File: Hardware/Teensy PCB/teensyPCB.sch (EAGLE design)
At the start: 16 parts, among them U1 HC_05, U2 USD-SOCKETNEW

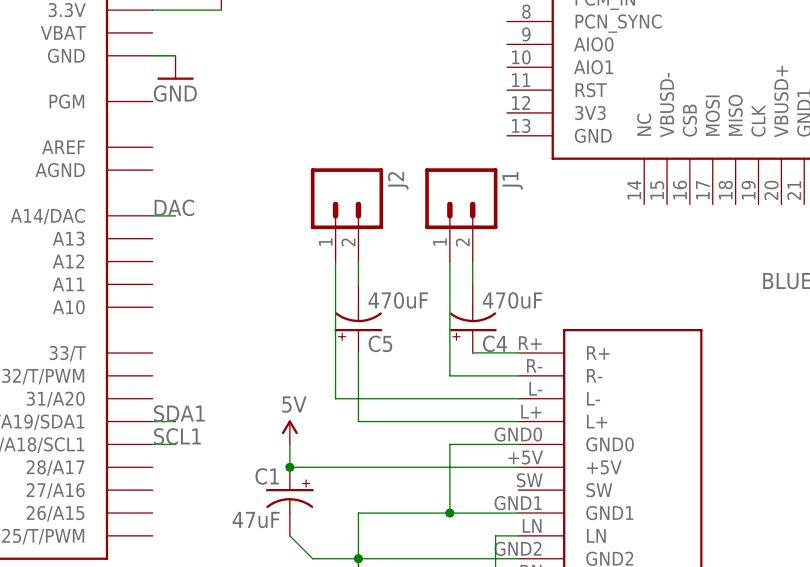
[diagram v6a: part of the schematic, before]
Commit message: Modified audio connections
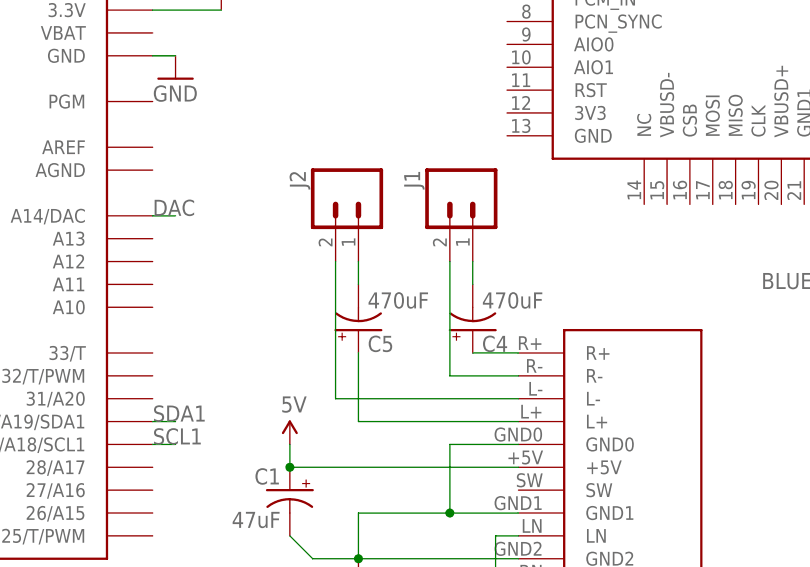
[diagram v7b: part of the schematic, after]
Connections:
- net N$3: now also C5.-, J2.1; no longer C4.-, J1.2
- net N$4: now also C4.-, J1.1; no longer C5.-, J2.2
- net N$6: now also J1.2; no longer J1.1
- net N$7: now also J2.2; no longer J2.1
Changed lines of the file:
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@@
 <setting verticaltext="up"/>
 </settings>
-<grid distance="0.1" unitdist="inch" unit="inch" style="lines" multiple="1" display="yes" altdistance="0.01" altunitdist="inch" altunit="inch"/>
+<grid distance="0.1" unitdist="inch" unit="inch" style="lines" multiple="1" display="no" altdistance="0.01" altunitdist="inch" altunit="inch"/>
 <layers>
 <layer number="1" name="Top" color="4" fill="1" visible="no" active="no"/>
@@
 <instance part="C2" gate="G$1" x="60.96" y="-35.56" rot="R90"/>
 <instance part="C3" gate="G$1" x="60.96" y="-43.18" rot="R90"/>
-<instance part="J1" gate="G$1" x="60.96" y="20.32" rot="R270"/>
-<instance part="J2" gate="G$1" x="48.26" y="20.32" rot="R270"/>
+<instance part="J1" gate="G$1" x="63.5" y="20.32" rot="MR270"/>
+<instance part="J2" gate="G$1" x="50.8" y="20.32" rot="MR270"/>
 <instance part="C4" gate="G$1" x="63.5" y="5.08" rot="MR180"/>
 <instance part="C5" gate="G$1" x="50.8" y="5.08" rot="MR180"/>
@@
 </segment>
 </net>
-<net name="N$3" class="0">
-<segment>
-<pinref part="J1" gate="G$1" pin="2"/>
-<pinref part="C4" gate="G$1" pin="-"/>
-<wire x1="63.5" y1="12.7" x2="63.5" y2="10.16" width="0.1524" layer="91"/>
-</segment>
-</net>
-<net name="N$4" class="0">
-<segment>
-<pinref part="J2" gate="G$1" pin="2"/>
-<pinref part="C5" gate="G$1" pin="-"/>
-<wire x1="50.8" y1="10.16" x2="50.8" y2="12.7" width="0.1524" layer="91"/>
-</segment>
-</net>
 <net name="N$5" class="0">
 <segment>
@@
 <net name="N$6" class="0">
 <segment>
-<pinref part="J1" gate="G$1" pin="1"/>
-<wire x1="60.96" y1="12.7" x2="60.96" y2="0" width="0.1524" layer="91"/>
 <pinref part="U$4" gate="G$1" pin="R-"/>
 <wire x1="60.96" y1="0" x2="68.58" y2="0" width="0.1524" layer="91"/>
+<pinref part="J1" gate="G$1" pin="2"/>
+<wire x1="60.96" y1="12.7" x2="60.96" y2="0" width="0.1524" layer="91"/>
 </segment>
 </net>
@@
 <segment>
 <pinref part="U$4" gate="G$1" pin="L-"/>
-<pinref part="J2" gate="G$1" pin="1"/>
 <wire x1="68.58" y1="-2.54" x2="48.26" y2="-2.54" width="0.1524" layer="91"/>
-<wire x1="48.26" y1="-2.54" x2="48.26" y2="12.7" width="0.1524" layer="91"/>
+<pinref part="J2" gate="G$1" pin="2"/>
+<wire x1="48.26" y1="12.7" x2="48.26" y2="-2.54" width="0.1524" layer="91"/>
 </segment>
 </net>
@@
 </segment>
 </net>
+<net name="N$3" class="0">
+<segment>
+<pinref part="C5" gate="G$1" pin="-"/>
+<pinref part="J2" gate="G$1" pin="1"/>
+<wire x1="50.8" y1="12.7" x2="50.8" y2="10.16" width="0.1524" layer="91"/>
+</segment>
+</net>
+<net name="N$4" class="0">
+<segment>
+<pinref part="C4" gate="G$1" pin="-"/>
+<pinref part="J1" gate="G$1" pin="1"/>
+<wire x1="63.5" y1="12.7" x2="63.5" y2="10.16" width="0.1524" layer="91"/>
+</segment>
+</net>

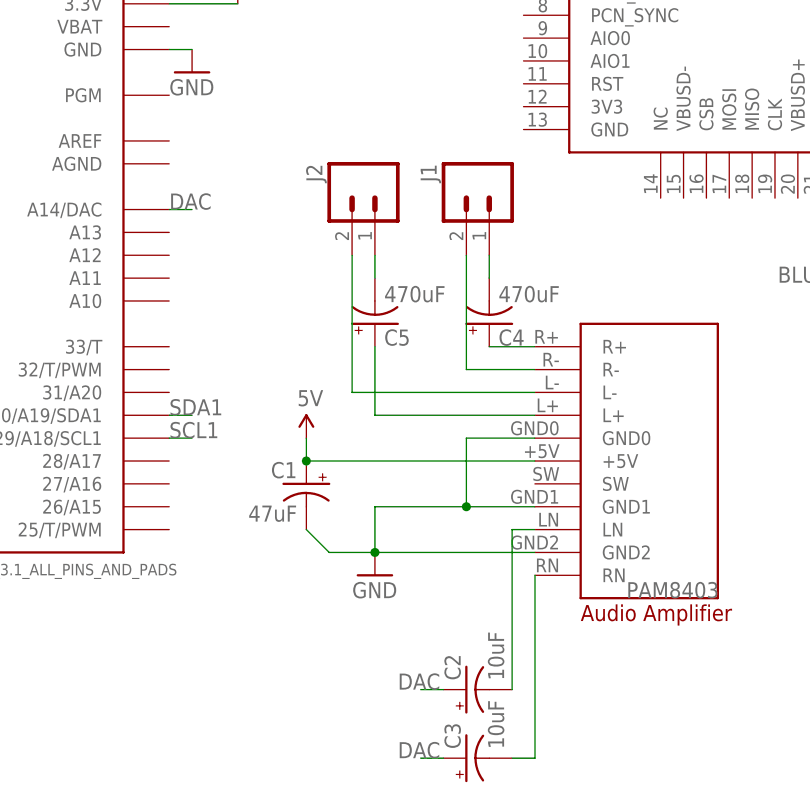
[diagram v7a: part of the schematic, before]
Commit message: Modified audio component
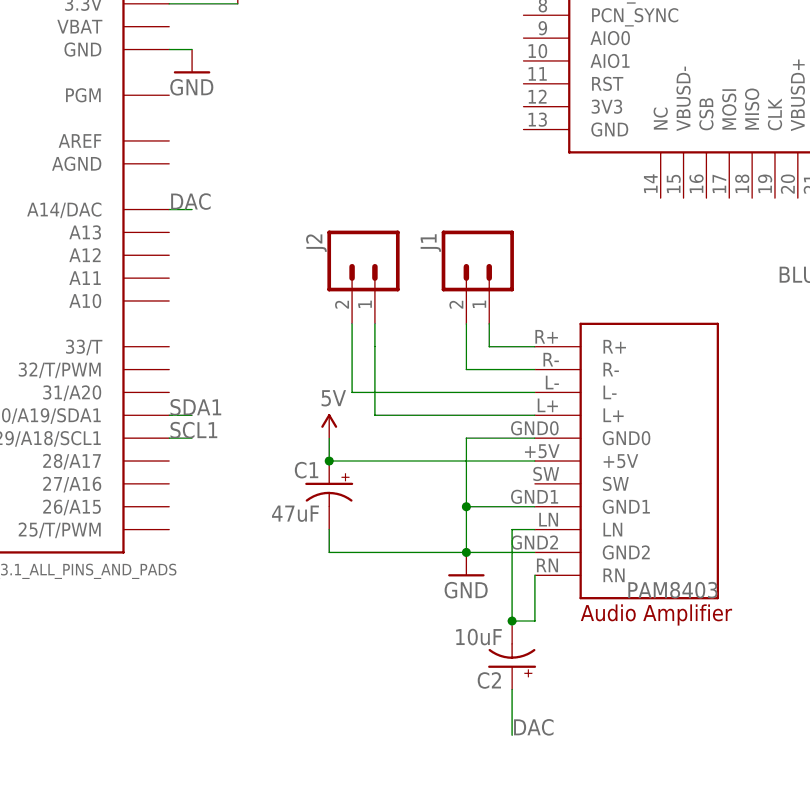
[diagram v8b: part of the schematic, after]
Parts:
- removed C3: 10uF, SparkFun-Capacitors:CAP_POL3528
- removed C4, C5: 470uF, SparkFun-Capacitors:CAP_POL3528
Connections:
- removed net N$2: C3.-, U$4.RN
- net DAC: no longer C3.+
- net N$1: now also U$4.RN
- net N$3: no longer C5.-
- net N$4: no longer C4.-
- net N$5: no longer C4.+
- net N$8: no longer C5.+
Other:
- moved on the sheet: C1, C2, J1, J2
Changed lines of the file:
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@@
 <part name="C1" library="SparkFun-Capacitors" deviceset="CAP_POL" device="3528" value="47uF"/>
 <part name="C2" library="SparkFun-Capacitors" deviceset="CAP_POL" device="3528" value="10uF"/>
-<part name="C3" library="SparkFun-Capacitors" deviceset="CAP_POL" device="3528" value="10uF"/>
 <part name="J1" library="SparkFun-Connectors" deviceset="M02" device="PTH"/>
 <part name="J2" library="SparkFun-Connectors" deviceset="M02" device="PTH"/>
-<part name="C4" library="SparkFun-Capacitors" deviceset="CAP_POL" device="3528" value="470uF"/>
-<part name="C5" library="SparkFun-Capacitors" deviceset="CAP_POL" device="3528" value="470uF"/>
 </parts>
 <sheets>
@@
 <instance part="SUPPLY6" gate="G$1" x="43.18" y="73.66" rot="R270"/>
 <instance part="GND6" gate="1" x="45.72" y="66.04" rot="R90"/>
-<instance part="SUPPLY7" gate="G$1" x="43.18" y="-7.62"/>
-<instance part="GND9" gate="1" x="50.8" y="-22.86"/>
+<instance part="SUPPLY7" gate="G$1" x="45.72" y="-7.62"/>
+<instance part="GND9" gate="1" x="60.96" y="-22.86"/>
 <instance part="U$4" gate="G$1" x="81.28" y="-10.16"/>
-<instance part="C1" gate="G$1" x="43.18" y="-12.7" rot="MR0"/>
-<instance part="C2" gate="G$1" x="60.96" y="-35.56" rot="R90"/>
-<instance part="C3" gate="G$1" x="60.96" y="-43.18" rot="R90"/>
-<instance part="J1" gate="G$1" x="63.5" y="20.32" rot="MR270"/>
-<instance part="J2" gate="G$1" x="50.8" y="20.32" rot="MR270"/>
-<instance part="C4" gate="G$1" x="63.5" y="5.08" rot="MR180"/>
-<instance part="C5" gate="G$1" x="50.8" y="5.08" rot="MR180"/>
+<instance part="C1" gate="G$1" x="45.72" y="-12.7" rot="MR0"/>
+<instance part="C2" gate="G$1" x="66.04" y="-33.02" rot="R180"/>
+<instance part="J1" gate="G$1" x="63.5" y="12.7" rot="MR270"/>
+<instance part="J2" gate="G$1" x="50.8" y="12.7" rot="MR270"/>
 </instances>
 <busses>
@@
 <pinref part="GND9" gate="1" pin="GND"/>
 <pinref part="U$4" gate="G$1" pin="GND2"/>
-<wire x1="50.8" y1="-20.32" x2="68.58" y2="-20.32" width="0.1524" layer="91"/>
+<wire x1="60.96" y1="-20.32" x2="68.58" y2="-20.32" width="0.1524" layer="91"/>
 <pinref part="U$4" gate="G$1" pin="GND1"/>
-<wire x1="50.8" y1="-15.24" x2="60.96" y2="-15.24" width="0.1524" layer="91"/>
 <wire x1="60.96" y1="-15.24" x2="68.58" y2="-15.24" width="0.1524" layer="91"/>
-<wire x1="50.8" y1="-15.24" x2="50.8" y2="-20.32" width="0.1524" layer="91"/>
-<junction x="50.8" y="-20.32"/>
+<wire x1="60.96" y1="-15.24" x2="60.96" y2="-20.32" width="0.1524" layer="91"/>
+<junction x="60.96" y="-20.32"/>
 <pinref part="C1" gate="G$1" pin="-"/>
-<wire x1="43.18" y1="-17.78" x2="45.72" y2="-20.32" width="0.1524" layer="91"/>
-<wire x1="45.72" y1="-20.32" x2="50.8" y2="-20.32" width="0.1524" layer="91"/>
+<wire x1="45.72" y1="-17.78" x2="45.72" y2="-20.32" width="0.1524" layer="91"/>
+<wire x1="45.72" y1="-20.32" x2="60.96" y2="-20.32" width="0.1524" layer="91"/>
 <pinref part="U$4" gate="G$1" pin="GND0"/>
 <wire x1="68.58" y1="-7.62" x2="60.96" y2="-7.62" width="0.1524" layer="91"/>
@@
 <pinref part="SUPPLY7" gate="G$1" pin="5V"/>
 <pinref part="U$4" gate="G$1" pin="+5V"/>
-<wire x1="43.18" y1="-10.16" x2="68.58" y2="-10.16" width="0.1524" layer="91"/>
+<wire x1="45.72" y1="-10.16" x2="68.58" y2="-10.16" width="0.1524" layer="91"/>
 <pinref part="C1" gate="G$1" pin="+"/>
-<junction x="43.18" y="-10.16"/>
-<wire x1="43.18" y1="-10.16" x2="43.18" y2="-7.62" width="0.1524" layer="91"/>
+<junction x="45.72" y="-10.16"/>
+<wire x1="45.72" y1="-10.16" x2="45.72" y2="-7.62" width="0.1524" layer="91"/>
 </segment>
 </net>
@@
 <pinref part="C2" gate="G$1" pin="-"/>
 <wire x1="68.58" y1="-17.78" x2="66.04" y2="-17.78" width="0.1524" layer="91"/>
-<wire x1="66.04" y1="-17.78" x2="66.04" y2="-35.56" width="0.1524" layer="91"/>
-</segment>
-</net>
-<net name="N$2" class="0">
-<segment>
+<wire x1="66.04" y1="-17.78" x2="66.04" y2="-27.94" width="0.1524" layer="91"/>
 <pinref part="U$4" gate="G$1" pin="RN"/>
-<wire x1="68.58" y1="-22.86" x2="68.58" y2="-43.18" width="0.1524" layer="91"/>
-<pinref part="C3" gate="G$1" pin="-"/>
-<wire x1="68.58" y1="-43.18" x2="66.04" y2="-43.18" width="0.1524" layer="91"/>
+<wire x1="68.58" y1="-22.86" x2="68.58" y2="-27.94" width="0.1524" layer="91"/>
+<wire x1="68.58" y1="-27.94" x2="66.04" y2="-27.94" width="0.1524" layer="91"/>
+<junction x="66.04" y="-27.94"/>
 </segment>
 </net>
@@
 <segment>
 <pinref part="C2" gate="G$1" pin="+"/>
-<wire x1="58.42" y1="-35.56" x2="55.88" y2="-35.56" width="0.1524" layer="91"/>
-<label x="53.34" y="-35.56" size="1.778" layer="95"/>
-</segment>
-<segment>
-<pinref part="C3" gate="G$1" pin="+"/>
-<wire x1="58.42" y1="-43.18" x2="55.88" y2="-43.18" width="0.1524" layer="91"/>
-<label x="53.34" y="-43.18" size="1.778" layer="95"/>
+<wire x1="66.04" y1="-35.56" x2="66.04" y2="-40.64" width="0.1524" layer="91"/>
+<label x="66.04" y="-40.64" size="1.778" layer="95"/>
 </segment>
 </net>
 <net name="N$5" class="0">
 <segment>
-<pinref part="C4" gate="G$1" pin="+"/>
 <pinref part="U$4" gate="G$1" pin="R+"/>
 <wire x1="63.5" y1="2.54" x2="68.58" y2="2.54" width="0.1524" layer="91"/>
@@
 <wire x1="60.96" y1="0" x2="68.58" y2="0" width="0.1524" layer="91"/>
 <pinref part="J1" gate="G$1" pin="2"/>
-<wire x1="60.96" y1="12.7" x2="60.96" y2="0" width="0.1524" layer="91"/>
+<wire x1="60.96" y1="5.08" x2="60.96" y2="0" width="0.1524" layer="91"/>
 </segment>
 </net>
@@
 <wire x1="68.58" y1="-2.54" x2="48.26" y2="-2.54" width="0.1524" layer="91"/>
 <pinref part="J2" gate="G$1" pin="2"/>
-<wire x1="48.26" y1="12.7" x2="48.26" y2="-2.54" width="0.1524" layer="91"/>
+<wire x1="48.26" y1="5.08" x2="48.26" y2="-2.54" width="0.1524" layer="91"/>
 </segment>
 </net>
 <net name="N$8" class="0">
 <segment>
-<pinref part="C5" gate="G$1" pin="+"/>
 <wire x1="50.8" y1="2.54" x2="50.8" y2="-5.08" width="0.1524" layer="91"/>
 <pinref part="U$4" gate="G$1" pin="L+"/>
@@
 <net name="N$3" class="0">
 <segment>
-<pinref part="C5" gate="G$1" pin="-"/>
 <pinref part="J2" gate="G$1" pin="1"/>
-<wire x1="50.8" y1="12.7" x2="50.8" y2="10.16" width="0.1524" layer="91"/>
+<wire x1="50.8" y1="5.08" x2="50.8" y2="2.54" width="0.1524" layer="91"/>
 </segment>
 </net>
 <net name="N$4" class="0">
 <segment>
-<pinref part="C4" gate="G$1" pin="-"/>
 <pinref part="J1" gate="G$1" pin="1"/>
-<wire x1="63.5" y1="12.7" x2="63.5" y2="10.16" width="0.1524" layer="91"/>
-</segment>
-</net>
+<wire x1="63.5" y1="5.08" x2="63.5" y2="2.54" width="0.1524" layer="91"/>
+</segment>
+</net>
